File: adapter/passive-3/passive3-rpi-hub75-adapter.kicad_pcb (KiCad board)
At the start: 2 copper layers, 80 x 23 mm, 6 parts, among them P1 CONN_02X20, P2 CONN_01X01, P3 CONN_01X01

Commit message: o Fix connection problem.
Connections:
- P1 pad 33: (no net) -> p1_g2
- P1 pad 36: (no net) -> p2_g2
- Panel-2 pad 6: (no net) -> p1_g2
- Panel-3 pad 6: (no net) -> p2_g2

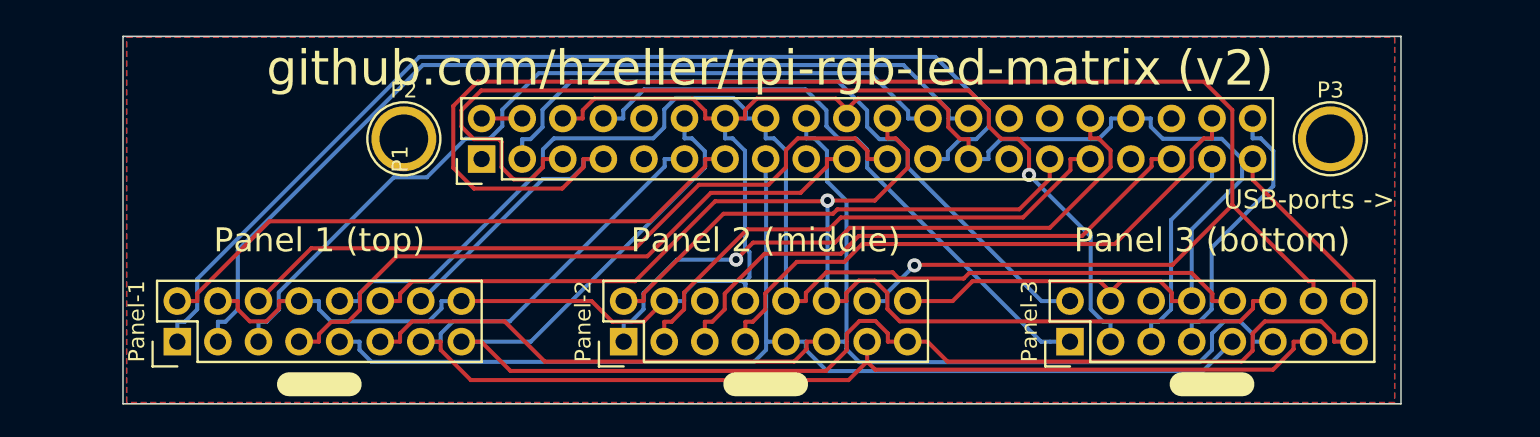
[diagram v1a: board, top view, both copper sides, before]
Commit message: o Route connections on board.
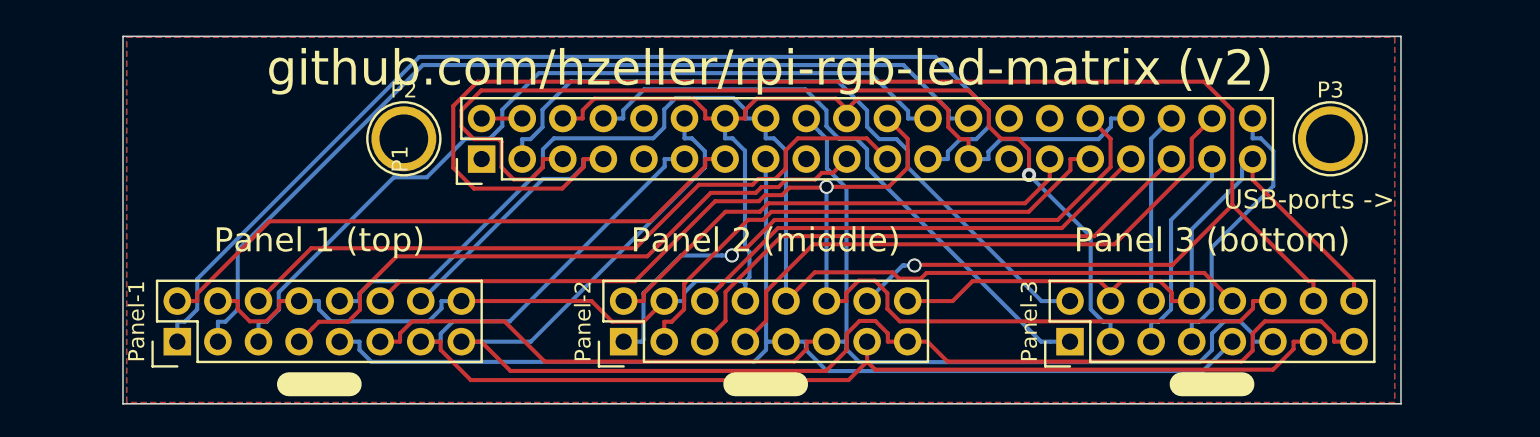
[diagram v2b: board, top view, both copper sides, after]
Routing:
- net p1_g2: track 0.00 -> 30.6 mm
- net p2_g2: track 0.00 -> 12.0 mm
- net GND: track 146.2 -> 137.9 mm
- net row_B: track 76.9 -> 76.3 mm
- net p0_b2: track 40.2 -> 39.6 mm
- net p1_b2: track 37.7 -> 37.1 mm
- net p1_r2: track 35.5 -> 35.0 mm
